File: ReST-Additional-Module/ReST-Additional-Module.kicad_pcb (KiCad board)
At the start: 2 copper layers, 25.5 x 33.5 mm, 6 parts, among them P1 CONN_02X07, P2 CONN_01X08, P3 CONN_02X04, P4 CONN_01X02, P5 CONN_01X02, U1 ULN2803

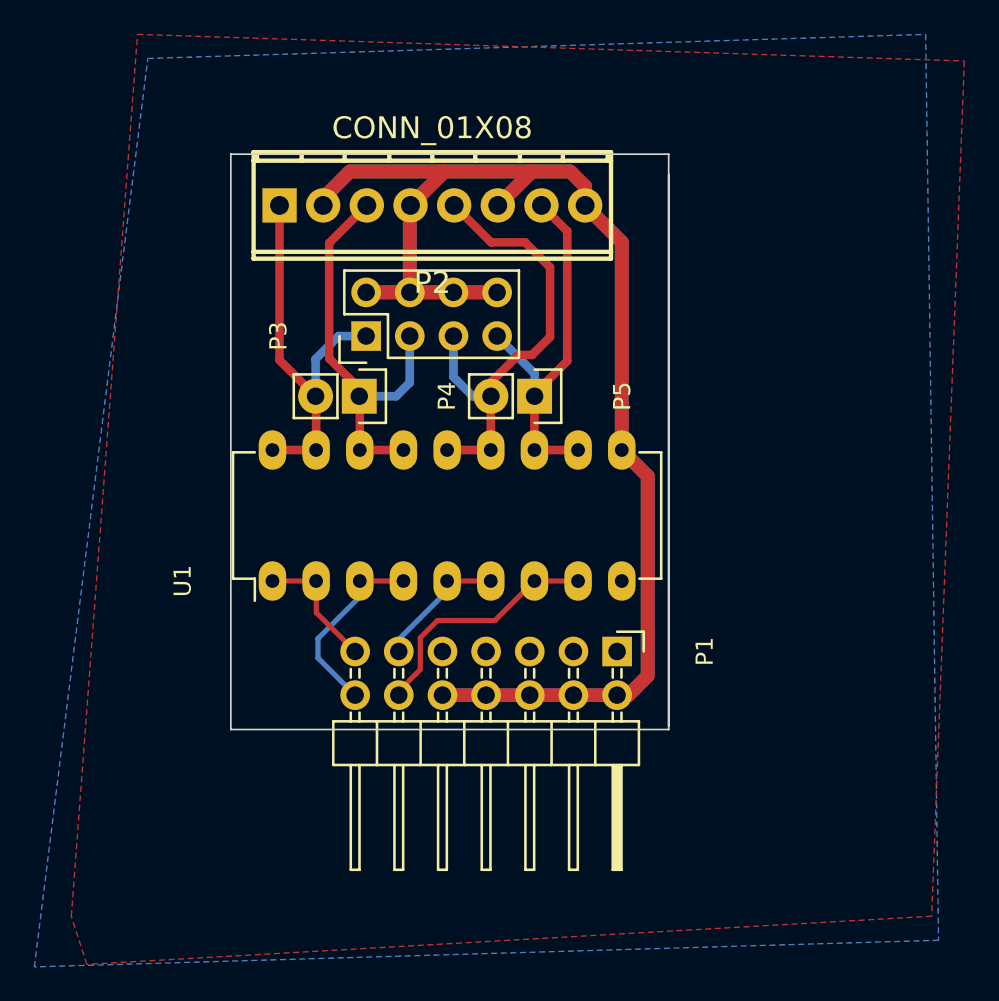
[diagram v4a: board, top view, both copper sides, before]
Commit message: Added Images and PDF's
+ Silkscreening
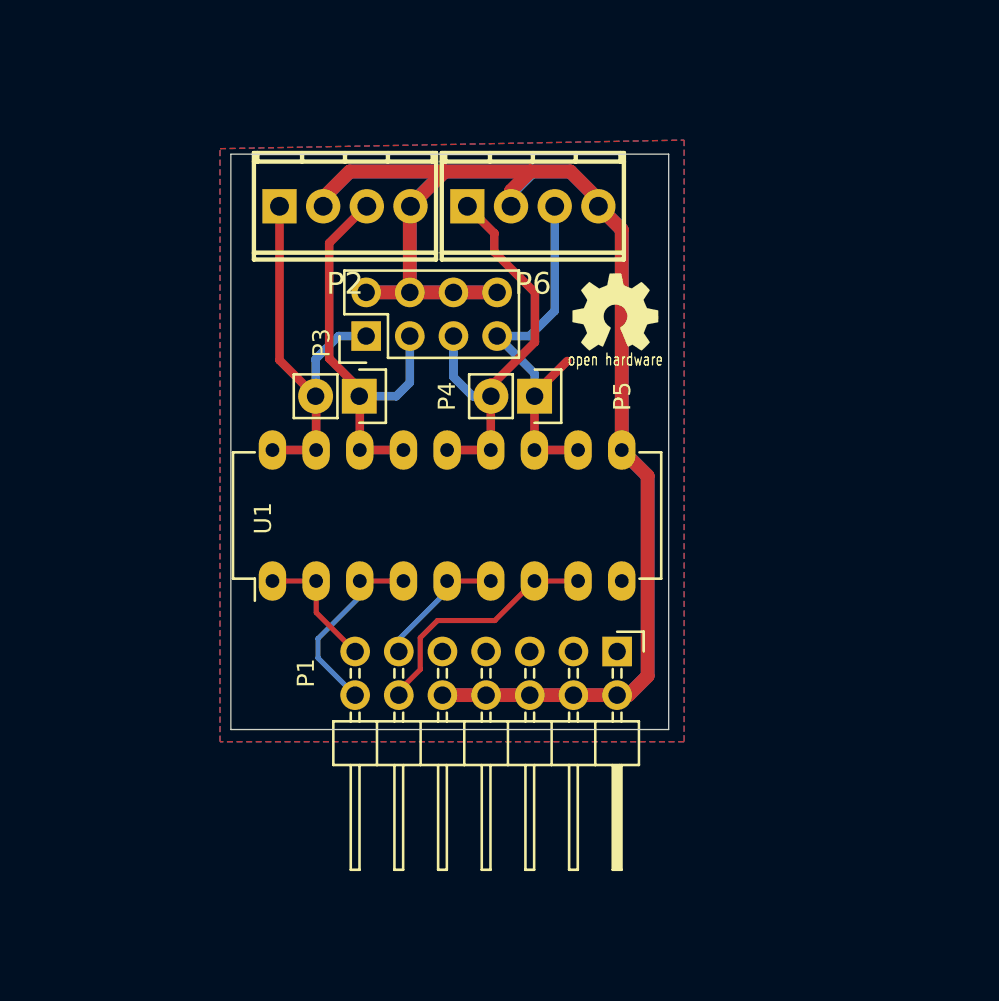
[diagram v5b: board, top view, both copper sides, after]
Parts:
- added G***: LOGO, ReST-Library:Logo_silk_OSHW_6x6mm, F.Cu at (158.5, 126.0)
- added G***: LOGO, ReST-Library:STM32, B.Cu at (157.0, 125.6)
- added P6: CONN_01X04, ReST-Library:screw-2,54-4P, F.Cu at (153.7, 119.8)
- P2: value CONN_01X08 -> CONN_01X04; footprint 2:mpt_0,5%2f8-2,54 -> ReST-Library:screw-2,54-4P
- moved P2 5.08 mm to (142.8, 119.8)
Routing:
- net /PWM-OUT2: track 27.2 -> 25.2 mm
- net +12V: track 154.9 -> 154.1 mm
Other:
- outline, holes or cut-outs redrawn
- board text added: "ReST32 Additional Module Rev. A | Test"
- board text added: "by Straw"

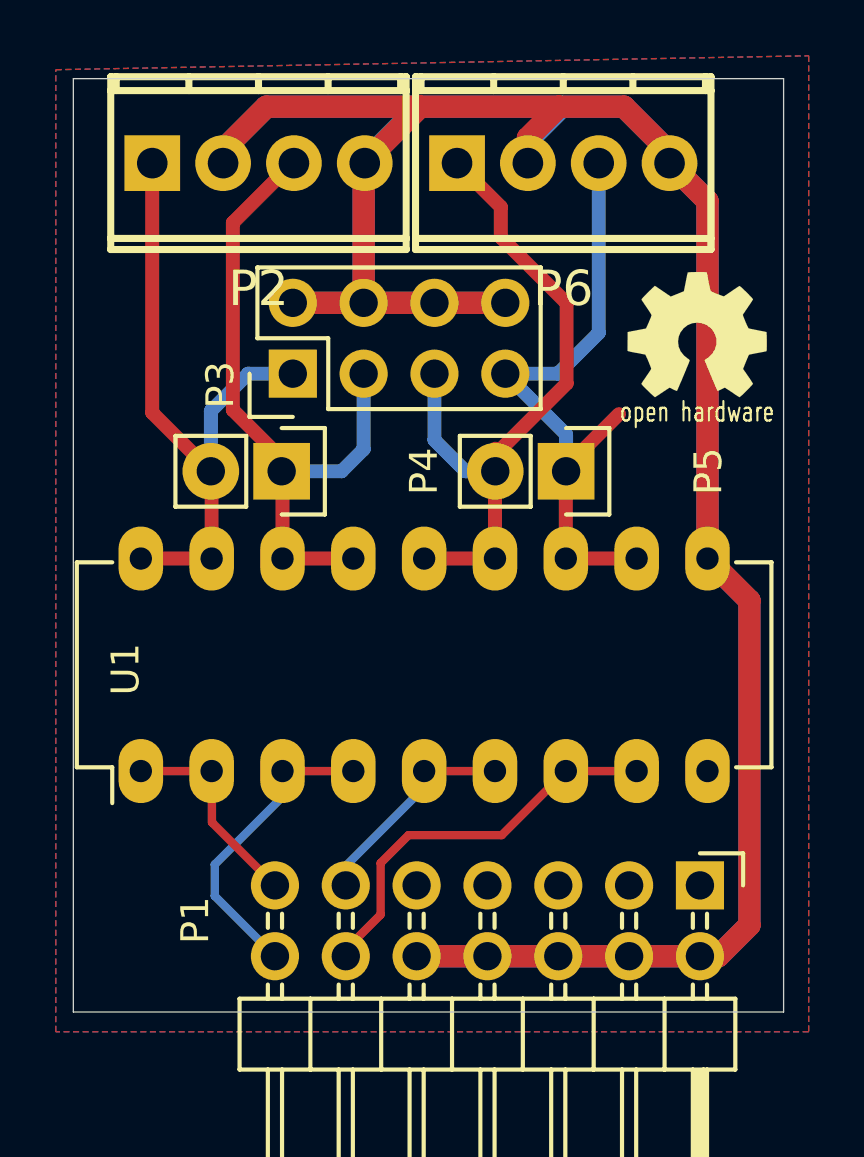
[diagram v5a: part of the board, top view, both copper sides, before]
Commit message: Added Mounting Holes to all Modules
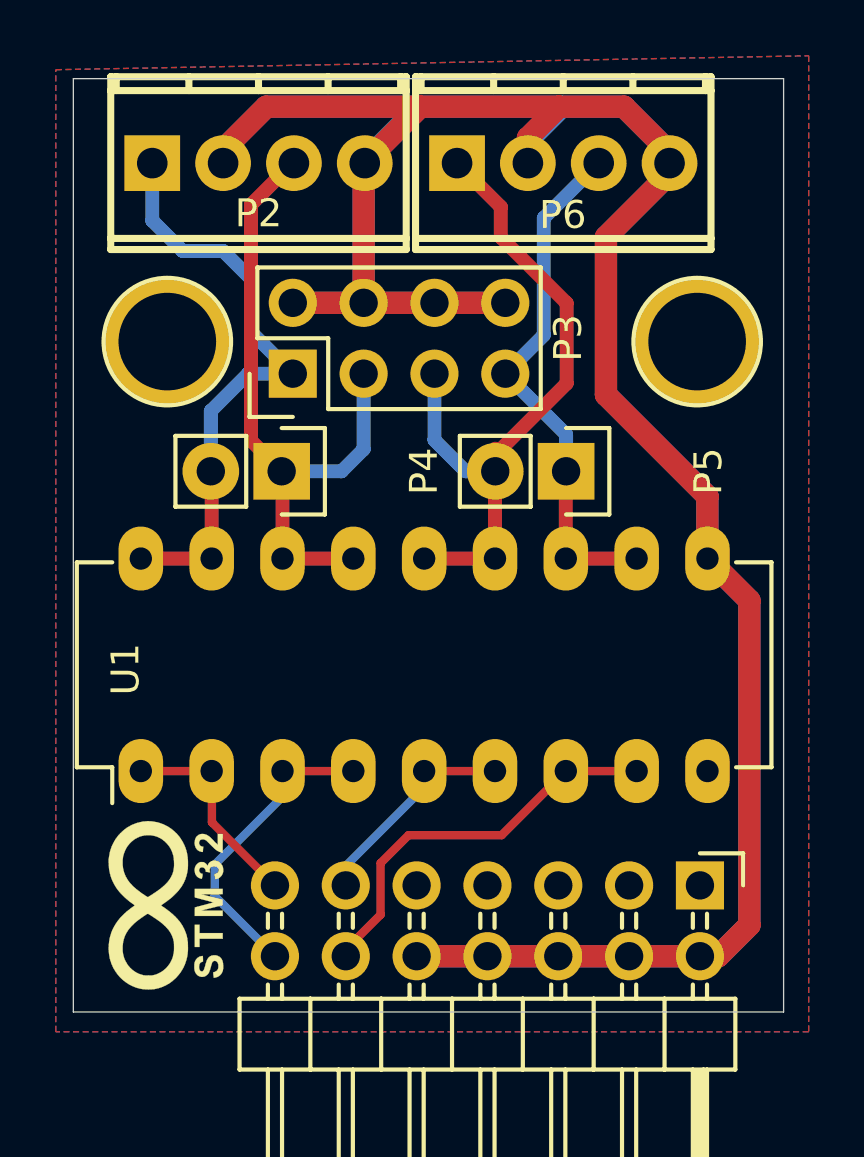
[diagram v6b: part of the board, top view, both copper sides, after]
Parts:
- added ?: , Connect:1pin, F.Cu at (158.5, 126.2)
- added ?: , Connect:1pin, F.Cu at (139.5, 126.2)
- G***: moved to B.Cu
- G***: moved to F.Cu
- moved G*** 27.8 mm to (139.4, 146.2), turned to 180 degrees
- moved G*** 27.2 mm to (139.5, 146.5), turned to 90 degrees
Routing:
- net /PWM-OUT3: track 23.0 -> 19.2 mm
- net +12V: track 154.1 -> 157.5 mm
- net /PWM-OUT0: track 23.3 -> 21.8 mm

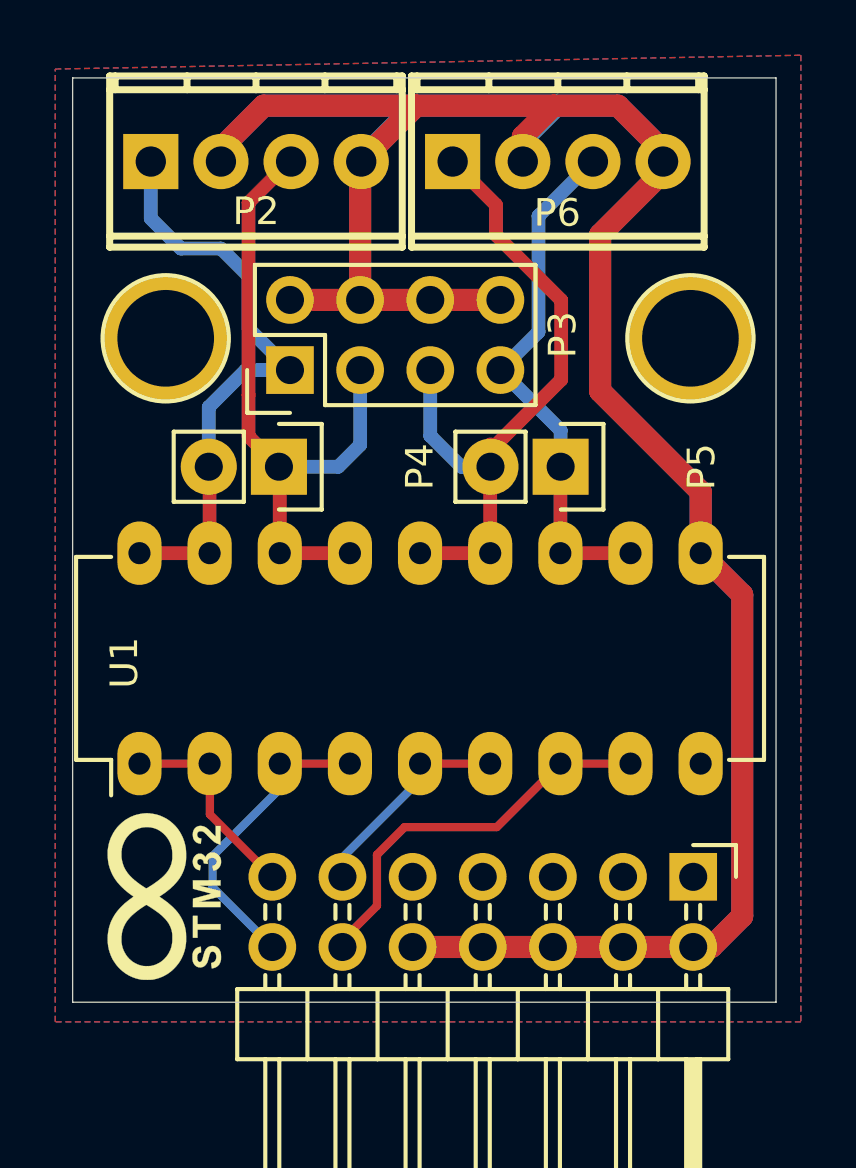
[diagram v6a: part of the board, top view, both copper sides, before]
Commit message: Finally removed all unnecessary Libs and added Heatsink for 5V Regulator
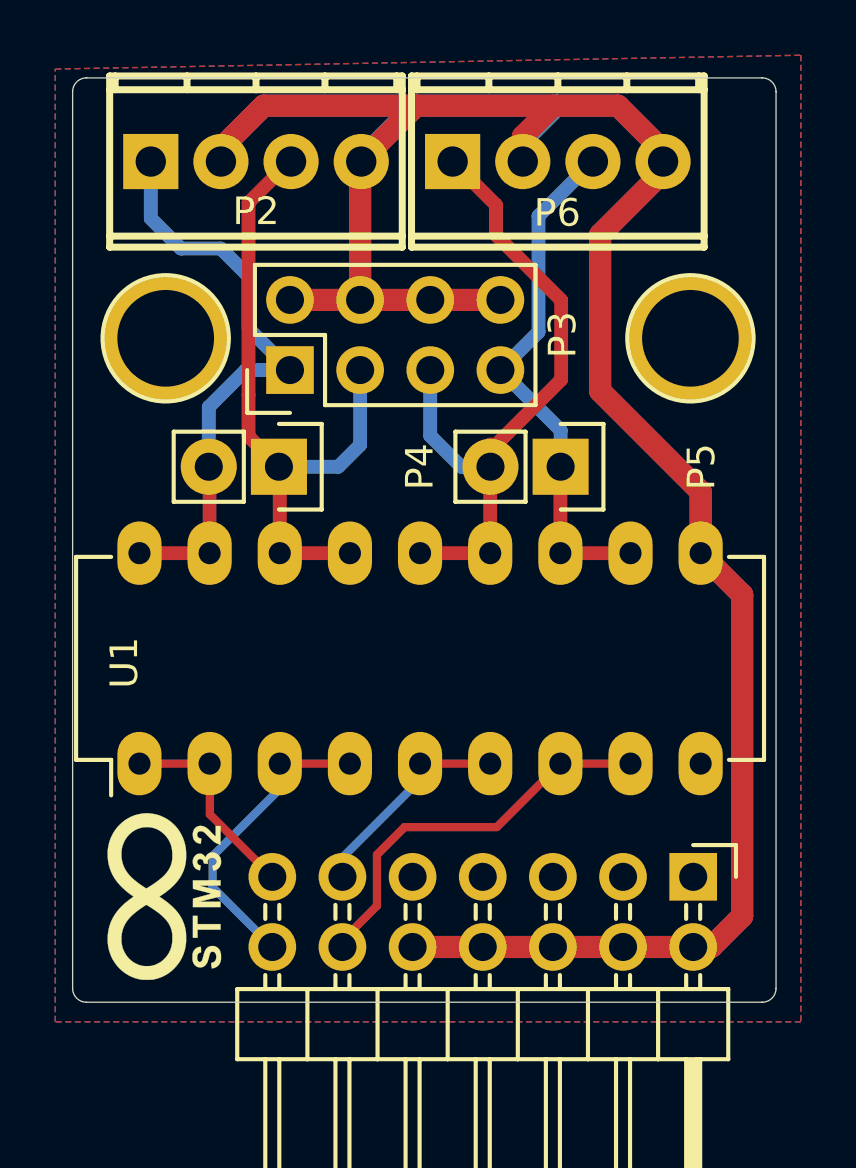
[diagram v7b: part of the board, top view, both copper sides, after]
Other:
- outline, holes or cut-outs redrawn
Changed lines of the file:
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@@
     (links 42)
     (no_connects 0)
-    (area 136.124999 116.814999 161.605001 150.295001)
+    (area 133.705 113.62512 162.675 159.175001)
     (thickness 1.6)
-    (drawings 6)
+    (drawings 10)
     (tracks 123)
     (zones 0)
@@
   )
   (setup
-    (last_trace_width 0.8)
+    (last_trace_width 0.25)
     (user_trace_width 0.3)
     (user_trace_width 0.5)
@@
     (trace_min 0.2)
     (segment_width 0.2)
-    (edge_width 0.1)
+    (edge_width 0.01)
     (via_size 0.6)
     (via_drill 0.4)
@@
     (pad 1 thru_hole circle (at 0 0) (size 4.5 4.5) (drill 3.5) (layers *.Cu *.Mask F.SilkS))
   )
+  (gr_arc (start 136.63 149.79) (end 136.63 150.29) (angle 90) (layer Edge.Cuts) (width 0.01))
+  (gr_arc (start 136.63 117.32) (end 136.13 117.32) (angle 90) (layer Edge.Cuts) (width 0.01))
+  (gr_arc (start 161.1 117.32) (end 161.1 116.82) (angle 90) (layer Edge.Cuts) (width 0.01))
+  (gr_arc (start 161.1 149.79) (end 161.6 149.79) (angle 90) (layer Edge.Cuts) (width 0.01))
+  (gr_line (start 136.63 150.29) (end 161.1 150.29) (angle 90) (layer Edge.Cuts) (width 0.01))
+  (gr_line (start 136.13 117.32) (end 136.13 149.79) (angle 90) (layer Edge.Cuts) (width 0.01))
+  (gr_line (start 161.1 116.82) (end 136.63 116.82) (angle 90) (layer Edge.Cuts) (width 0.01))
+  (gr_line (start 161.6 149.79) (end 161.6 117.32) (angle 90) (layer Edge.Cuts) (width 0.01))
   (gr_text "by Straw" (at 142 139) (layer B.SilkS)
     (effects (font (size 0.7 0.7) (thickness 0.175)) (justify mirror))
@@
     (effects (font (size 1 1) (thickness 0.2)) (justify left mirror))
   )
-  (gr_line (start 136.13 116.82) (end 136.13 150.29) (angle 90) (layer Edge.Cuts) (width 0.01))
-  (gr_line (start 161.6 116.82) (end 136.13 116.82) (angle 90) (layer Edge.Cuts) (width 0.01))
-  (gr_line (start 161.6 150.29) (end 161.6 116.82) (angle 90) (layer Edge.Cuts) (width 0.01))
-  (gr_line (start 136.13 150.29) (end 161.6 150.29) (angle 90) (layer Edge.Cuts) (width 0.01))
   (segment (start 157.51 119.85) (end 157.51 120.22) (width 0.8) (layer F.Cu) (net 2))
   (segment (start 157.51 120.22) (end 155.23 122.5) (width 0.8) (layer F.Cu) (net 2))
